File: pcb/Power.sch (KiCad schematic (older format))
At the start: 19 parts, among them J5 PWR5V, Q4 PMV160UP, Q5 PMV160UP, Q6 2N7002, Q7 2N7002, U2 AD8000YRDZ, U3 THS3001DGN

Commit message: Removed old comment from schematic
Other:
- note removed: "To use basic linear regulator, jumper pins 1-2 and 4-5.\nTo power externally, supply +5V to pin 1 and -5V to pin 5."
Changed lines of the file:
@@
 	-1   0    0    -1
 $EndComp
-Text Notes 2350 4800 0    60   ~ 0
-To use basic linear regulator, jumper pins 1-2 and 4-5.\nTo power externally, supply +5V to pin 1 and -5V to pin 5.
 $Comp
 L PMV160UP Q4

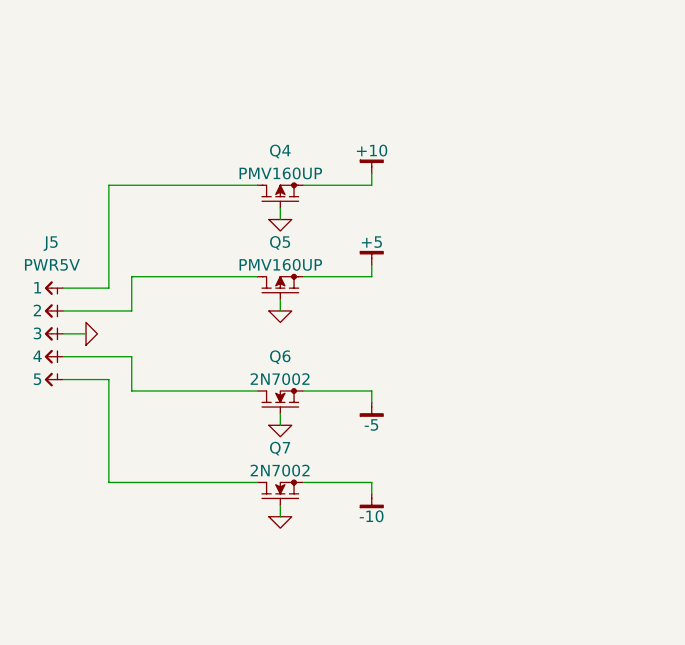
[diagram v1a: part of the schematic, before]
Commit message: Fixed FET part numbers
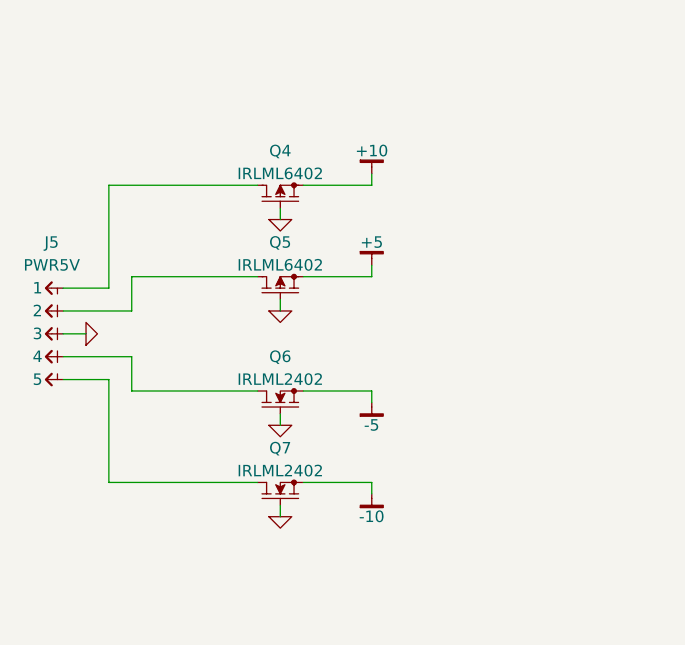
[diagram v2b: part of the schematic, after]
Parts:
- Q4, Q5: value PMV160UP -> IRLML6402
- Q6, Q7: value 2N7002 -> IRLML2402
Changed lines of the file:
@@
 EESchema Schematic File Version 2
-LIBS:vishay_semi
 LIBS:texas
-LIBS:symbol
 LIBS:supertex
-LIBS:st_semi
-LIBS:st_ic
-LIBS:skyworks
-LIBS:silabs
-LIBS:semi
-LIBS:russian-nixies
-LIBS:resistors
 LIBS:power
-LIBS:passive
-LIBS:onsemi
-LIBS:nxp_semi
-LIBS:nxp_ic
 LIBS:microchip
-LIBS:mechanical
-LIBS:maxim
-LIBS:ltc
-LIBS:lattice
-LIBS:ixys
-LIBS:irf
-LIBS:intersil
-LIBS:infineon
-LIBS:inductors
-LIBS:ic_template
 LIBS:ftdi
-LIBS:fairchild_semi
-LIBS:fairchild_ic
-LIBS:electromech
 LIBS:display
-LIBS:diodesinc
 LIBS:conn
-LIBS:capacitors
 LIBS:atmel
-LIBS:altera
-LIBS:ad
-LIBS:7400
-LIBS:4000
-LIBS:2N-SMD
-LIBS:2N
-LIBS:1N-SMD
-LIBS:1N
 LIBS:wcp52-output-cache
 EELAYER 25 0
@@
 P 3350 2900
 F 0 "Q4" V 3550 2900 50  0000 C CNN
-F 1 "PMV160UP" V 3450 2900 50  0000 C CNN
+F 1 "IRLML6402" V 3450 2900 50  0000 C CNN
 F 2 "IPC-semi-nominal:SOT-23" H 3350 2900 60  0001 C CNN
 F 3 "" H 3350 2900 60  0000 C CNN
@@
 P 3350 3300
 F 0 "Q5" V 3550 3300 50  0000 C CNN
-F 1 "PMV160UP" V 3450 3300 50  0000 C CNN
+F 1 "IRLML6402" V 3450 3300 50  0000 C CNN
 F 2 "IPC-semi-nominal:SOT-23" H 3350 3300 60  0001 C CNN
 F 3 "" H 3350 3300 60  0000 C CNN
@@
 P 3350 3800
 F 0 "Q6" V 3550 3800 50  0000 C CNN
-F 1 "2N7002" V 3450 3800 50  0000 C CNN
+F 1 "IRLML2402" V 3450 3800 50  0000 C CNN
 F 2 "IPC-semi-nominal:SOT-23" H 3350 3800 60  0001 C CNN
 F 3 "" H 3350 3800 60  0000 C CNN
@@
 P 3350 4200
 F 0 "Q7" V 3550 4200 50  0000 C CNN
-F 1 "2N7002" V 3450 4200 50  0000 C CNN
+F 1 "IRLML2402" V 3450 4200 50  0000 C CNN
 F 2 "IPC-semi-nominal:SOT-23" H 3350 4200 60  0001 C CNN
 F 3 "" H 3350 4200 60  0000 C CNN
